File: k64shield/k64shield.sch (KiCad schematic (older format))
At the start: 7 parts, among them J1 top_left_header_02x08, J2 bottom_left_header_02x06, J3 rpi_motor_driver_header, J4 top_right_header_02x10, J5 bottom_right_header_02x08, J6 camera_header_01x05, J7 servo_header_01x03

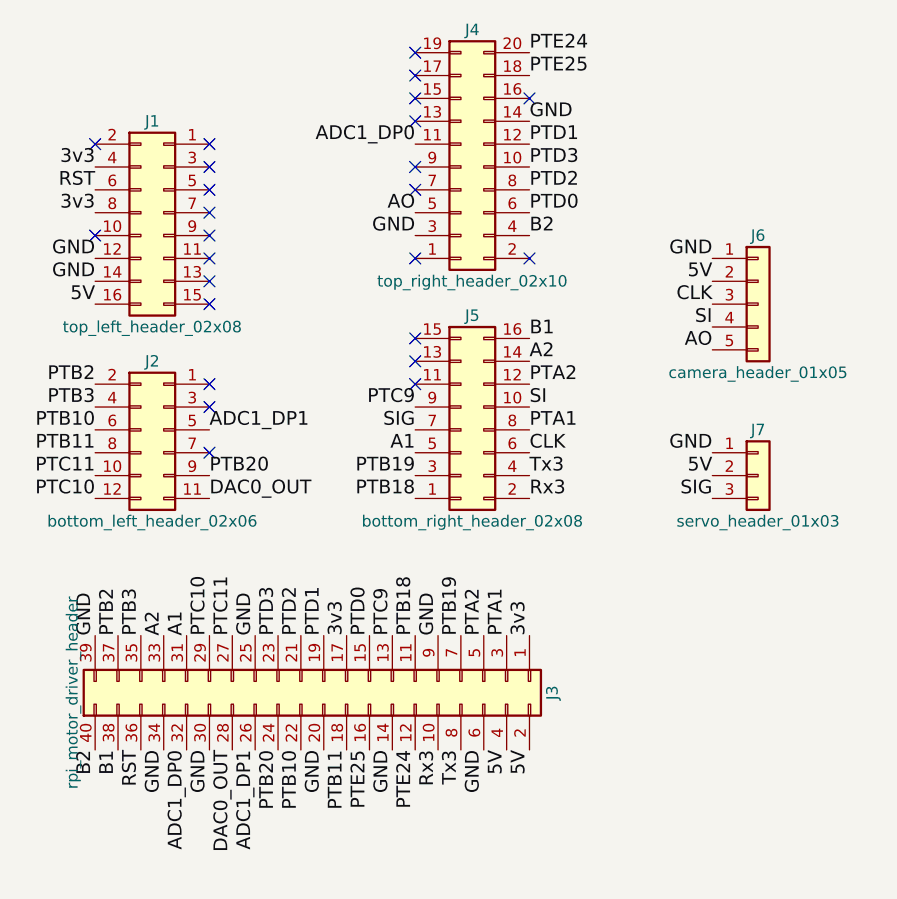
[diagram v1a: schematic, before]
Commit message: Fixed all wiring. Everything is connected on PCB
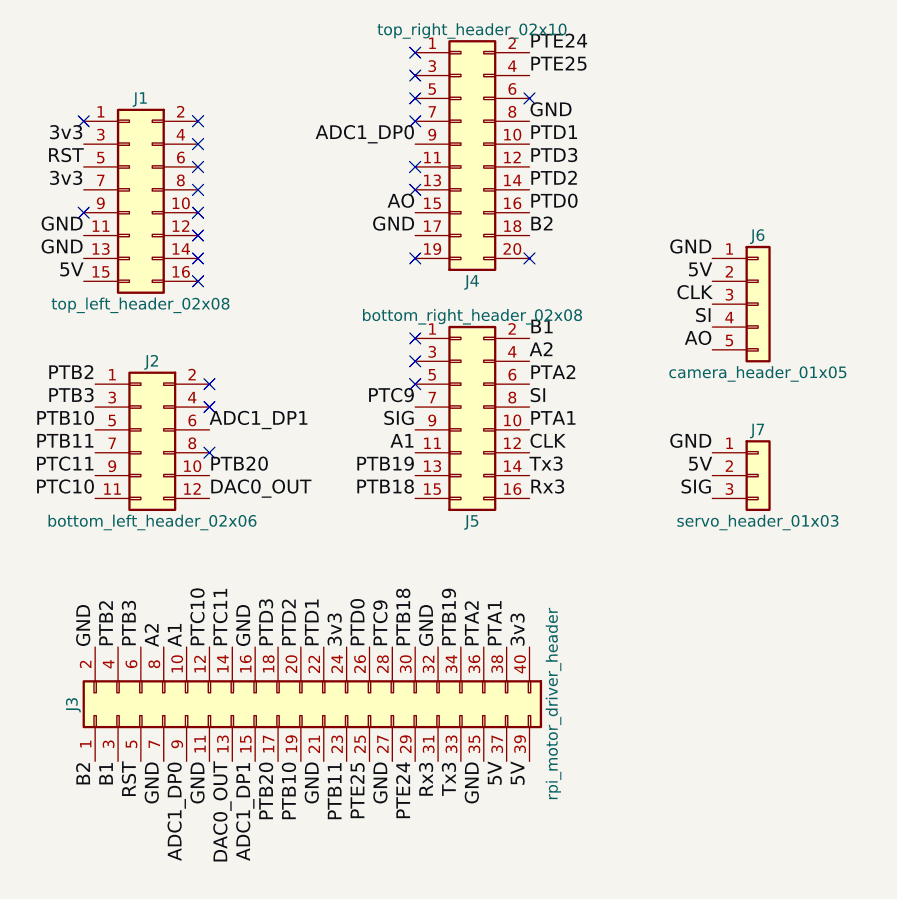
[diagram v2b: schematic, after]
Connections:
- net 3v3: now also J1.3 (NC-3), J1.7 (NC-7), J3.24 (CE0-24), J3.40 (P29-40); no longer J1.4 (P3V3-4), J1.8 (P3V3-8), J3.1 (3v3-1), J3.17 (3v3-17)
- net 5V: now also J1.15 (NC-15), J3.37 (P25-37), J3.39 (GND-39); no longer J1.16 (P5-9_VIN-16), J3.2 (5v-2), J3.4 (5v-4)
- net A1: now also J3.10 (RX-10), J5.11 (PTC0-11); no longer J3.31 (P22-31), J5.5 (PTC1-5)
- net A2: now also J3.8 (TX-8), J5.4 (PTC17-4); no longer J3.33 (P23-33), J5.14 (PTC2-14)
- net ADC1_DP0: now also J3.9 (GND-9), J4.9 (NC-9); no longer J3.32 (P26-32), J4.11 (ADC1_DP0-11)
- net ADC1_DP1: now also J2.6 (PTB10-6), J3.15 (P3-15); no longer J2.5 (ADC1_DP1-5), J3.26 (CE1-26)
- net AO: now also J4.15 (NC-15); no longer J4.5 (ADC0_DP0-5)
- net B1: now also J3.3 (SDA-3), J5.2 (PTC16-2); no longer J3.38 (P28-38), J5.16 (PTC3-16)
- net B2: now also J3.1 (3v3-1), J4.18 (PTE25-18); no longer J3.40 (P29-40), J4.4 (PTC4-4)
- net CLK: now also J5.12 (PTA2-12); no longer J5.6 (PTB9-6)
- net DAC0_OUT: now also J2.12 (PTC10-12), J3.13 (P2-13); no longer J2.11 (DAC0_OUT-11), J3.28 (IDSC-28)
- net GND: now also J1.11 (NC-11), J1.13 (NC-13), J3.11 (P0-11), J3.16 (P4-16), J3.2 (5v-2), J3.21 (MISO-21), J3.27 (IDSO-27), J3.32 (P26-32), J3.35 (P24-35), J3.7 (P7-7), J4.17 (ADC1_SE18-17), J4.8 (PTD2-8); no longer J1.12 (GND-12), J1.14 (GND-14), J3.14 (GND-14), J3.20 (GND-20), J3.25 (GND-25), J3.30 (GND-30), J3.34 (GND-34), J3.39 (GND-39), J3.6 (GND-6), J3.9 (GND-9), J4.14 (GND-14), J4.3 (GND-3)
- net PTA1: now also J3.38 (P28-38), J5.10 (PTB23-10); no longer J3.3 (SDA-3), J5.8 (PTA1-8)
- net PTA2: now also J3.36 (P27-36), J5.6 (PTB9-6); no longer J3.5 (SCL-5), J5.12 (PTA2-12)
- net PTB10: now also J2.5 (ADC1_DP1-5), J3.19 (MOSI-19); no longer J2.6 (PTB10-6), J3.22 (P6-22)
- net PTB11: now also J2.7 (ADC1_DM1-7), J3.23 (SCK-23); no longer J2.8 (PTB11-8), J3.18 (P5-18)
- net PTB18: now also J3.30 (GND-30), J5.15 (PTC5-15); no longer J3.11 (P0-11), J5.1 (PTB18-1)
- net PTB19: now also J3.34 (GND-34), J5.13 (PTC7-13); no longer J3.7 (P7-7), J5.3 (PTB19-3)
- net PTB2: now also J2.1 (ADC0_DP1-1), J3.4 (5v-4); no longer J2.2 (PTB2-2), J3.37 (P25-37)
- net PTB20: now also J2.10 (PTC11-10), J3.17 (3v3-17); no longer J2.9 (PTB20-9), J3.24 (CE0-24)
- net PTB3: now also J2.3 (ADC0_DM1-3), J3.6 (GND-6); no longer J2.4 (PTB3-4), J3.35 (P24-35)
- net PTC10: now also J2.11 (DAC0_OUT-11), J3.12 (P1-12); no longer J2.12 (PTC10-12), J3.29 (P21-29)
- net PTC11: now also J2.9 (PTB20-9), J3.14 (GND-14); no longer J2.10 (PTC11-10), J3.27 (IDSO-27)
- net PTC9: now also J3.28 (IDSC-28), J5.7 (PTC8-7); no longer J3.13 (P2-13), J5.9 (PTC9-9)
- net PTD0: now also J3.26 (CE1-26), J4.16 (AREF-16); no longer J3.15 (P3-15), J4.6 (PTD0-6)
- net PTD1: now also J3.22 (P6-22), J4.10 (PTD3-10); no longer J3.19 (MOSI-19), J4.12 (PTD1-12)
- net PTD2: now also J3.20 (GND-20), J4.14 (GND-14); no longer J3.21 (MISO-21), J4.8 (PTD2-8)
- net PTD3: now also J3.18 (P5-18), J4.12 (PTD1-12); no longer J3.23 (SCK-23), J4.10 (PTD3-10)
- net PTE24: now also J3.29 (P21-29), J4.2 (PTC12-2); no longer J3.12 (P1-12), J4.20 (PTE24-20)
- net PTE25: now also J3.25 (GND-25), J4.4 (PTC4-4); no longer J3.16 (P4-16), J4.18 (PTE25-18)
- net RST: now also J1.5 (NC-5), J3.5 (SCL-5); no longer J1.6 (RESET-6), J3.36 (P27-36)
- net Rx3: now also J3.31 (P22-31), J5.16 (PTC3-16); no longer J3.10 (RX-10), J5.2 (PTC16-2)
- net SI: now also J5.8 (PTA1-8); no longer J5.10 (PTB23-10)
- net SIG: now also J5.9 (PTC9-9); no longer J5.7 (PTC8-7)
- net Tx3: now also J3.33 (P23-33), J5.14 (PTC2-14); no longer J3.8 (TX-8), J5.4 (PTC17-4)
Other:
- moved on the sheet: J1, J3
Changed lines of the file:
@@
 L top_left_header_02x08 J1
 U 1 1 5BEBC742
-P 6100 2850
-F 0 "J1" H 6150 3250 50  0000 C CNN
-F 1 "top_left_header_02x08" H 6150 2350 50  0000 C CNN
-F 2 "Pin_Headers:Pin_Header_Straight_2x08_Pitch2.54mm" H 6100 2850 50  0001 C CNN
-F 3 "" H 6100 2850 50  0001 C CNN
-	1    6100 2850
-	1    0    0    -1
+P 6150 2750
+F 0 "J1" H 6200 3150 50  0000 C CNN
+F 1 "top_left_header_02x08" H 6200 2250 50  0000 C CNN
+F 2 "Pin_Headers:Pin_Header_Straight_2x08_Pitch2.54mm" H 6150 2750 50  0001 C CNN
+F 3 "" H 6150 2750 50  0001 C CNN
+	1    6150 2750
+	-1   0    0    -1
 $EndComp
 $Comp
 L bottom_left_header_02x06 J2
 U 1 1 5BEBC80A
-P 6100 3800
-F 0 "J2" H 6150 4100 50  0000 C CNN
-F 1 "bottom_left_header_02x06" H 6150 3400 50  0000 C CNN
-F 2 "Pin_Headers:Pin_Header_Straight_2x06_Pitch2.54mm" H 6100 3800 50  0001 C CNN
-F 3 "" H 6100 3800 50  0001 C CNN
-	1    6100 3800
-	1    0    0    -1
+P 6200 3800
+F 0 "J2" H 6250 4100 50  0000 C CNN
+F 1 "bottom_left_header_02x06" H 6250 3400 50  0000 C CNN
+F 2 "Pin_Headers:Pin_Header_Straight_2x06_Pitch2.54mm" H 6200 3800 50  0001 C CNN
+F 3 "" H 6200 3800 50  0001 C CNN
+	1    6200 3800
+	-1   0    0    -1
 $EndComp
 $Comp
 L top_right_header_02x10 J4
 U 1 1 5BEBC857
-P 7500 2550
-F 0 "J4" H 7550 3050 50  0000 C CNN
-F 1 "top_right_header_02x10" H 7550 1950 50  0000 C CNN
-F 2 "Pin_Headers:Pin_Header_Straight_2x10_Pitch2.54mm" H 7500 2550 50  0001 C CNN
-F 3 "" H 7500 2550 50  0001 C CNN
-	1    7500 2550
-	1    0    0    -1
+P 7500 2650
+F 0 "J4" H 7550 3150 50  0000 C CNN
+F 1 "top_right_header_02x10" H 7550 2050 50  0000 C CNN
+F 2 "Pin_Headers:Pin_Header_Straight_2x10_Pitch2.54mm" H 7500 2650 50  0001 C CNN
+F 3 "" H 7500 2650 50  0001 C CNN
+	1    7500 2650
+	1    0    0    1
 $EndComp
 $Comp
 L bottom_right_header_02x08 J5
 U 1 1 5BEBCB19
-P 7500 3700
-F 0 "J5" H 7550 4100 50  0000 C CNN
-F 1 "bottom_right_header_02x08" H 7550 3200 50  0000 C CNN
-F 2 "Pin_Headers:Pin_Header_Straight_2x08_Pitch2.54mm" H 7500 3700 50  0001 C CNN
-F 3 "" H 7500 3700 50  0001 C CNN
-	1    7500 3700
-	1    0    0    -1
+P 7500 3800
+F 0 "J5" H 7550 4200 50  0000 C CNN
+F 1 "bottom_right_header_02x08" H 7550 3300 50  0000 C CNN
+F 2 "Pin_Headers:Pin_Header_Straight_2x08_Pitch2.54mm" H 7500 3800 50  0001 C CNN
+F 3 "" H 7500 3800 50  0001 C CNN
+	1    7500 3800
+	1    0    0    1
 $EndComp
 $Comp
 L rpi_motor_driver_header J3
 U 1 1 5BEBCC38
-P 6750 4950
-F 0 "J3" H 6750 6100 50  0000 C CNN
-F 1 "rpi_motor_driver_header" H 6750 4000 50  0000 C CNN
-F 2 "Pin_Headers:Pin_Header_Straight_2x20_Pitch2.54mm" H 6800 5000 50  0001 C CNN
-F 3 "" H 6800 5000 50  0001 C CNN
-	1    6750 4950
-	0    1    1    0
-$EndComp
-Text Label 6300 4700 1    60   ~ 0
+P 6950 5000
+F 0 "J3" H 6950 6150 50  0000 C CNN
+F 1 "rpi_motor_driver_header" H 6950 4050 50  0000 C CNN
+F 2 "Pin_Headers:Pin_Header_Straight_2x20_Pitch2.54mm" H 7000 5050 50  0001 C CNN
+F 3 "" H 7000 5050 50  0001 C CNN
+	1    6950 5000
+	0    -1   -1   0
+$EndComp
+Text Label 6300 4750 1    60   ~ 0
 A1
 Text Label 7300 3900 2    60   ~ 0
 A1
-Text Label 6200 4700 1    60   ~ 0
+Text Label 6200 4750 1    60   ~ 0
 A2
 Text Label 7800 3500 0    60   ~ 0
 A2
-Text Label 6000 5200 3    60   ~ 0
+Text Label 6000 5250 3    60   ~ 0
 B1
 Text Label 7800 3400 0    60   ~ 0
 B1
-Text Label 5900 5200 3    60   ~ 0
+Text Label 5900 5250 3    60   ~ 0
 B2
 Text Label 7800 2950 0    60   ~ 0
@@
 Text Label 8600 3150 2    60   ~ 0
 5V
-Text Label 7800 5200 3    60   ~ 0
+Text Label 7800 5250 3    60   ~ 0
 5V
 Text Label 8600 3250 2    60   ~ 0
@@
 	1    0    0    -1
 $EndComp
-Text Label 5900 3250 2    60   ~ 0
-5V
-Text Label 5900 3050 2    60   ~ 0
-GND
-Text Label 5900 3150 2    60   ~ 0
+Text Label 5850 3150 2    60   ~ 0
+5V
+Text Label 5850 2950 2    60   ~ 0
+GND
+Text Label 5850 3050 2    60   ~ 0
 GND
 Text Label 7800 2450 0    60   ~ 0
 GND
-Text Label 5900 4700 1    60   ~ 0
-GND
-Text Label 6200 5200 3    60   ~ 0
-GND
-Text Label 6600 4700 1    60   ~ 0
-GND
-Text Label 7400 4700 1    60   ~ 0
-GND
-Text Label 7600 5200 3    60   ~ 0
-GND
-Text Label 7200 5200 3    60   ~ 0
-GND
-Text Label 6900 5200 3    60   ~ 0
-GND
-Text Label 6400 5200 3    60   ~ 0
-GND
-Text Label 7700 5200 3    60   ~ 0
+Text Label 5900 4750 1    60   ~ 0
+GND
+Text Label 6200 5250 3    60   ~ 0
+GND
+Text Label 6600 4750 1    60   ~ 0
+GND
+Text Label 7400 4750 1    60   ~ 0
+GND
+Text Label 7600 5250 3    60   ~ 0
+GND
+Text Label 7200 5250 3    60   ~ 0
+GND
+Text Label 6900 5250 3    60   ~ 0
+GND
+Text Label 6400 5250 3    60   ~ 0
+GND
+Text Label 7700 5250 3    60   ~ 0
 5V
 Text Label 8600 4000 2    60   ~ 0
@@
 Text Label 7300 3800 2    60   ~ 0
 SIG
-NoConn ~ 5900 2550
-NoConn ~ 5900 2950
-NoConn ~ 6400 2550
-NoConn ~ 6400 2650
-NoConn ~ 6400 2750
-NoConn ~ 6400 2850
-NoConn ~ 6400 2950
-NoConn ~ 6400 3050
-NoConn ~ 6400 3150
-NoConn ~ 6400 3250
+NoConn ~ 5850 2450
+NoConn ~ 5850 2850
+NoConn ~ 6350 2450
+NoConn ~ 6350 2550
+NoConn ~ 6350 2650
+NoConn ~ 6350 2750
+NoConn ~ 6350 2850
+NoConn ~ 6350 2950
+NoConn ~ 6350 3050
+NoConn ~ 6350 3150
 NoConn ~ 6400 3900
 NoConn ~ 6400 3700
@@
 Text Label 7800 4100 0    60   ~ 0
 Rx3
-Text Label 7400 5200 3    60   ~ 0
+Text Label 7400 5250 3    60   ~ 0
 Rx3
 Text Label 7800 4000 0    60   ~ 0
 Tx3
-Text Label 7500 5200 3    60   ~ 0
+Text Label 7500 5250 3    60   ~ 0
 Tx3
-Text Label 5900 2650 2    60   ~ 0
-3v3
-Text Label 5900 2850 2    60   ~ 0
-3v3
-Text Label 7800 4700 1    60   ~ 0
-3v3
-Text Label 7000 4700 1    60   ~ 0
+Text Label 5850 2550 2    60   ~ 0
+3v3
+Text Label 5850 2750 2    60   ~ 0
+3v3
+Text Label 7800 4750 1    60   ~ 0
+3v3
+Text Label 7000 4750 1    60   ~ 0
 3v3
 Text Label 7800 3800 0    60   ~ 0
 PTA1
-Text Label 7700 4700 1    60   ~ 0
+Text Label 7700 4750 1    60   ~ 0
 PTA1
 Text Label 7800 3600 0    60   ~ 0
 PTA2
-Text Label 7600 4700 1    60   ~ 0
+Text Label 7600 4750 1    60   ~ 0
 PTA2
 Text Label 5900 3600 2    60   ~ 0
 PTB2
-Text Label 6000 4700 1    60   ~ 0
+Text Label 6000 4750 1    60   ~ 0
 PTB2
 Text Label 5900 3700 2    60   ~ 0
 PTB3
-Text Label 6100 4700 1    60   ~ 0
+Text Label 6100 4750 1    60   ~ 0
 PTB3
 Text Label 7300 4000 2    60   ~ 0
 PTB19
-Text Label 7500 4700 1    60   ~ 0
+Text Label 7500 4750 1    60   ~ 0
 PTB19
 Text Label 7300 4100 2    60   ~ 0
 PTB18
-Text Label 7300 4700 1    60   ~ 0
+Text Label 7300 4750 1    60   ~ 0
 PTB18
 Text Label 7300 3700 2    60   ~ 0
 PTC9
-Text Label 7200 4700 1    60   ~ 0
+Text Label 7200 4750 1    60   ~ 0
 PTC9
 Text Label 5900 4100 2    60   ~ 0
 PTC10
-Text Label 6400 4700 1    60   ~ 0
+Text Label 6400 4750 1    60   ~ 0
 PTC10
 Text Label 5900 4000 2    60   ~ 0
 PTC11
-Text Label 6500 4700 1    60   ~ 0
+Text Label 6500 4750 1    60   ~ 0
 PTC11
 Text Label 7800 2850 0    60   ~ 0
 PTD0
-Text Label 7100 4700 1    60   ~ 0
+Text Label 7100 4750 1    60   ~ 0
 PTD0
 Text Label 7800 2550 0    60   ~ 0
 PTD1
-Text Label 6900 4700 1    60   ~ 0
+Text Label 6900 4750 1    60   ~ 0
 PTD1
 Text Label 7800 2750 0    60   ~ 0
 PTD2
-Text Label 6800 4700 1    60   ~ 0
+Text Label 6800 4750 1    60   ~ 0
 PTD2
 Text Label 7800 2650 0    60   ~ 0
 PTD3
-Text Label 6700 4700 1    60   ~ 0
+Text Label 6700 4750 1    60   ~ 0
 PTD3
 Text Label 7800 2150 0    60   ~ 0
 PTE24
-Text Label 7300 5200 3    60   ~ 0
+Text Label 7300 5250 3    60   ~ 0
 PTE24
 Text Label 7800 2250 0    60   ~ 0
 PTE25
-Text Label 7100 5200 3    60   ~ 0
+Text Label 7100 5250 3    60   ~ 0
 PTE25
-Text Label 5900 2750 2    60   ~ 0
+Text Label 5850 2650 2    60   ~ 0
 RST
-Text Label 6100 5200 3    60   ~ 0
+Text Label 6100 5250 3    60   ~ 0
 RST
 Text Label 7300 2550 2    60   ~ 0
 ADC1_DP0
-Text Label 6300 5200 3    60   ~ 0
+Text Label 6300 5250 3    60   ~ 0
 ADC1_DP0
 Text Label 6400 4100 0    60   ~ 0
 DAC0_OUT
-Text Label 6500 5200 3    60   ~ 0
+Text Label 6500 5250 3    60   ~ 0
 DAC0_OUT
 Text Label 6400 3800 0    60   ~ 0
 ADC1_DP1
-Text Label 6600 5200 3    60   ~ 0
+Text Label 6600 5250 3    60   ~ 0
 ADC1_DP1
 Text Label 6400 4000 0    60   ~ 0
 PTB20
-Text Label 6700 5200 3    60   ~ 0
+Text Label 6700 5250 3    60   ~ 0
 PTB20
 Text Label 5900 3800 2    60   ~ 0
 PTB10
-Text Label 6800 5200 3    60   ~ 0
+Text Label 6800 5250 3    60   ~ 0
 PTB10
-Text Label 7000 5200 3    60   ~ 0
+Text Label 7000 5250 3    60   ~ 0
 PTB11
 Text Label 5900 3900 2    60   ~ 0

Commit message: Working
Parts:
- J1: symbol top_left_header_02x08 -> k64_pin:top_left_header_02x08
- J2: symbol bottom_left_header_02x06 -> k64_pin:bottom_left_header_02x06
- J3: symbol rpi_motor_driver_header -> k64_pin:rpi_motor_driver_header
- J4: symbol top_right_header_02x10 -> k64_pin:top_right_header_02x10
- J5: symbol bottom_right_header_02x08 -> k64_pin:bottom_right_header_02x08
- J6: symbol camera_header_01x05 -> k64_pin:camera_header_01x05
- J7: symbol servo_header_01x03 -> k64_pin:servo_header_01x03
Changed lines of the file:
@@
-EESchema Schematic File Version 2
-LIBS:power
-LIBS:device
-LIBS:switches
-LIBS:relays
-LIBS:motors
-LIBS:transistors
-LIBS:conn
-LIBS:linear
-LIBS:regul
-LIBS:74xx
-LIBS:cmos4000
-LIBS:adc-dac
-LIBS:memory
-LIBS:xilinx
-LIBS:microcontrollers
-LIBS:dsp
-LIBS:microchip
-LIBS:analog_switches
-LIBS:motorola
-LIBS:texas
-LIBS:intel
-LIBS:audio
-LIBS:interface
-LIBS:digital-audio
-LIBS:philips
-LIBS:display
-LIBS:cypress
-LIBS:siliconi
-LIBS:opto
-LIBS:atmel
-LIBS:contrib
-LIBS:valves
-LIBS:k64_pin
+EESchema Schematic File Version 4
 LIBS:k64shield-cache
-EELAYER 25 0
+EELAYER 26 0
 EELAYER END
 $Descr A4 11693 8268
@@
 $EndDescr
 $Comp
-L top_left_header_02x08 J1
+L k64_pin:top_left_header_02x08 J1
 U 1 1 5BEBC742
 P 6150 2750
@@
 $EndComp
 $Comp
-L bottom_left_header_02x06 J2
+L k64_pin:bottom_left_header_02x06 J2
 U 1 1 5BEBC80A
 P 6200 3800
@@
 $EndComp
 $Comp
-L top_right_header_02x10 J4
+L k64_pin:top_right_header_02x10 J4
 U 1 1 5BEBC857
 P 7500 2650
@@
 $EndComp
 $Comp
-L bottom_right_header_02x08 J5
+L k64_pin:bottom_right_header_02x08 J5
 U 1 1 5BEBCB19
 P 7500 3800
@@
 $EndComp
 $Comp
-L rpi_motor_driver_header J3
+L k64_pin:rpi_motor_driver_header J3
 U 1 1 5BEBCC38
 P 6950 5000
@@
 B2
 $Comp
-L camera_header_01x05 J6
+L k64_pin:camera_header_01x05 J6
 U 1 1 5BEBD558
 P 8800 3250
@@
 AO
 $Comp
-L servo_header_01x03 J7
+L k64_pin:servo_header_01x03 J7
 U 1 1 5BEBE0BE
 P 8800 4000

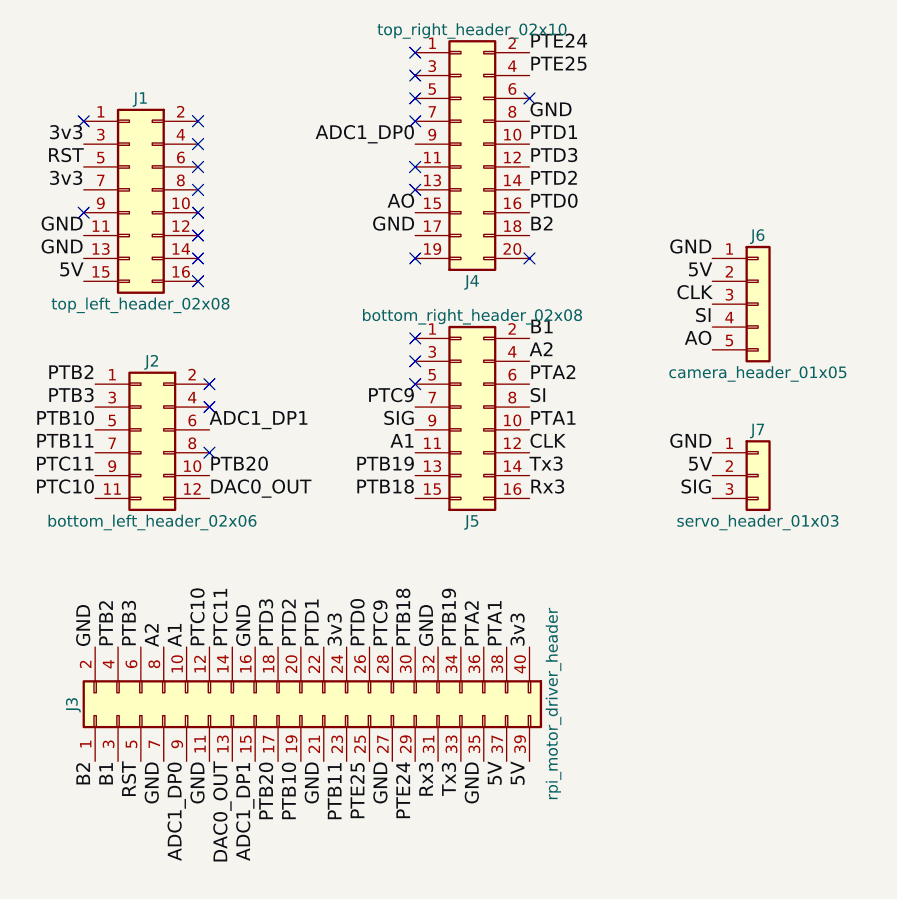
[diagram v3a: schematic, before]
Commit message: moved pins so enable were connected to gpio
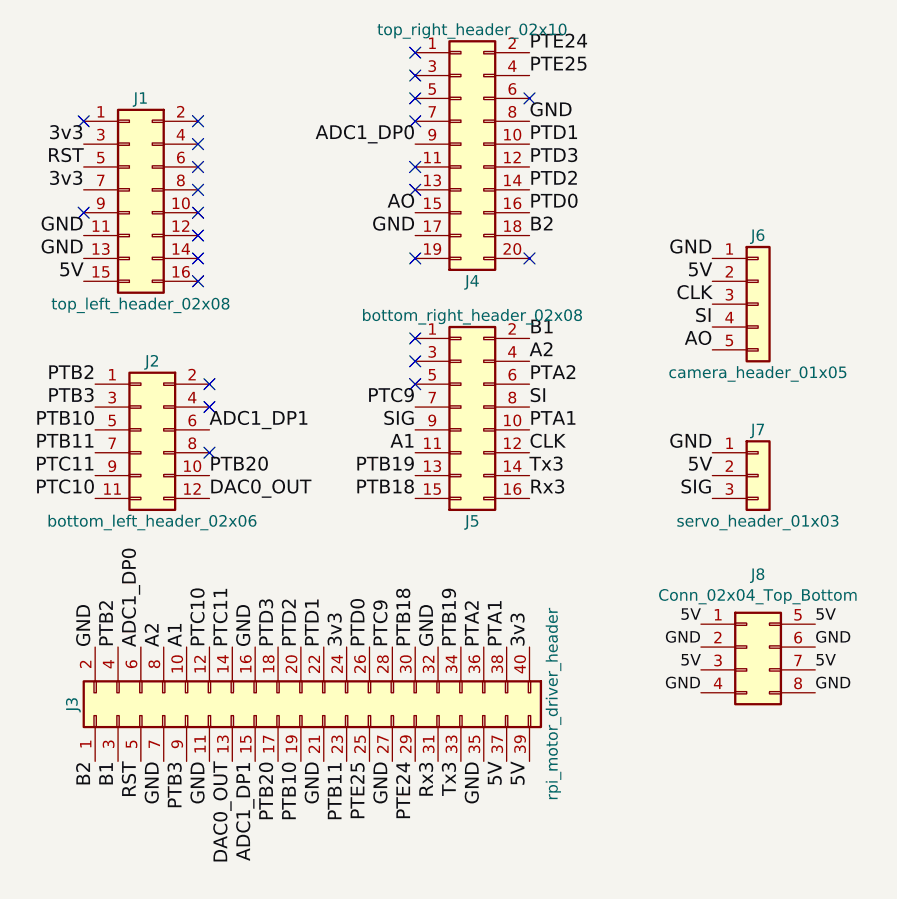
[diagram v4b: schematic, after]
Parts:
- added J8: Conn_02x04_Top_Bottom, Pin_Headers:Pin_Header_Straight_2x04_Pitch2.54mm, symbol Connector_Generic:Conn_02x04_Top_Bottom
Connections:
- net 5V: now also J8.1 (Pin_1), J8.3 (Pin_3), J8.5 (Pin_5), J8.7 (Pin_7)
- net ADC1_DP0: now also J3.6 (GND-6); no longer J3.9 (GND-9)
- net GND: now also J8.2 (Pin_2), J8.4 (Pin_4), J8.6 (Pin_6), J8.8 (Pin_8)
- net PTB3: now also J3.9 (GND-9); no longer J3.6 (GND-6)
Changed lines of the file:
@@
 Text Label 5900 3700 2    60   ~ 0
 PTB3
-Text Label 6100 4750 1    60   ~ 0
+Text Label 6300 5250 3    60   ~ 0
 PTB3
 Text Label 7300 4000 2    60   ~ 0
@@
 Text Label 7300 2550 2    60   ~ 0
 ADC1_DP0
-Text Label 6300 5250 3    60   ~ 0
+Text Label 6100 4750 1    60   ~ 0
 ADC1_DP0
 Text Label 6400 4100 0    60   ~ 0
@@
 Text Label 5900 3900 2    60   ~ 0
 PTB11
+$Comp
+L Connector_Generic:Conn_02x04_Top_Bottom J8
+U 1 1 5BF3F075
+P 8750 4750
+F 0 "J8" H 8800 5067 50  0000 C CNN
+F 1 "Conn_02x04_Top_Bottom" H 8800 4976 50  0000 C CNN
+F 2 "Pin_Headers:Pin_Header_Straight_2x04_Pitch2.54mm" H 8750 4750 50  0001 C CNN
+F 3 "~" H 8750 4750 50  0001 C CNN
+	1    8750 4750
+	1    0    0    -1
+$EndComp
+Text Label 8550 4650 2    50   ~ 0
+5V
+Text Label 9050 4650 0    50   ~ 0
+5V
+Text Label 8550 4850 2    50   ~ 0
+5V
+Text Label 9050 4850 0    50   ~ 0
+5V
+Text Label 8550 4750 2    50   ~ 0
+GND
+Text Label 9050 4750 0    50   ~ 0
+GND
+Text Label 9050 4950 0    50   ~ 0
+GND
+Text Label 8550 4950 2    50   ~ 0
+GND
 $EndSCHEMATC
